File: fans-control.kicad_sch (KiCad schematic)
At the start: 47 parts, among them J2 PinHeader_1x4_P2.5mm_Drill1mm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, J3 PinHeader_1x4_P2.5mm_Drill1mm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, J4 PinHeader_1x4_P2.5mm_Drill1mm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, J5 PinHeader_1x4_P2.5mm_Drill1mm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, Q4 BSS138PW, U5 LM339_TSSOP_Split, U6 TS5A3359_VSSOP

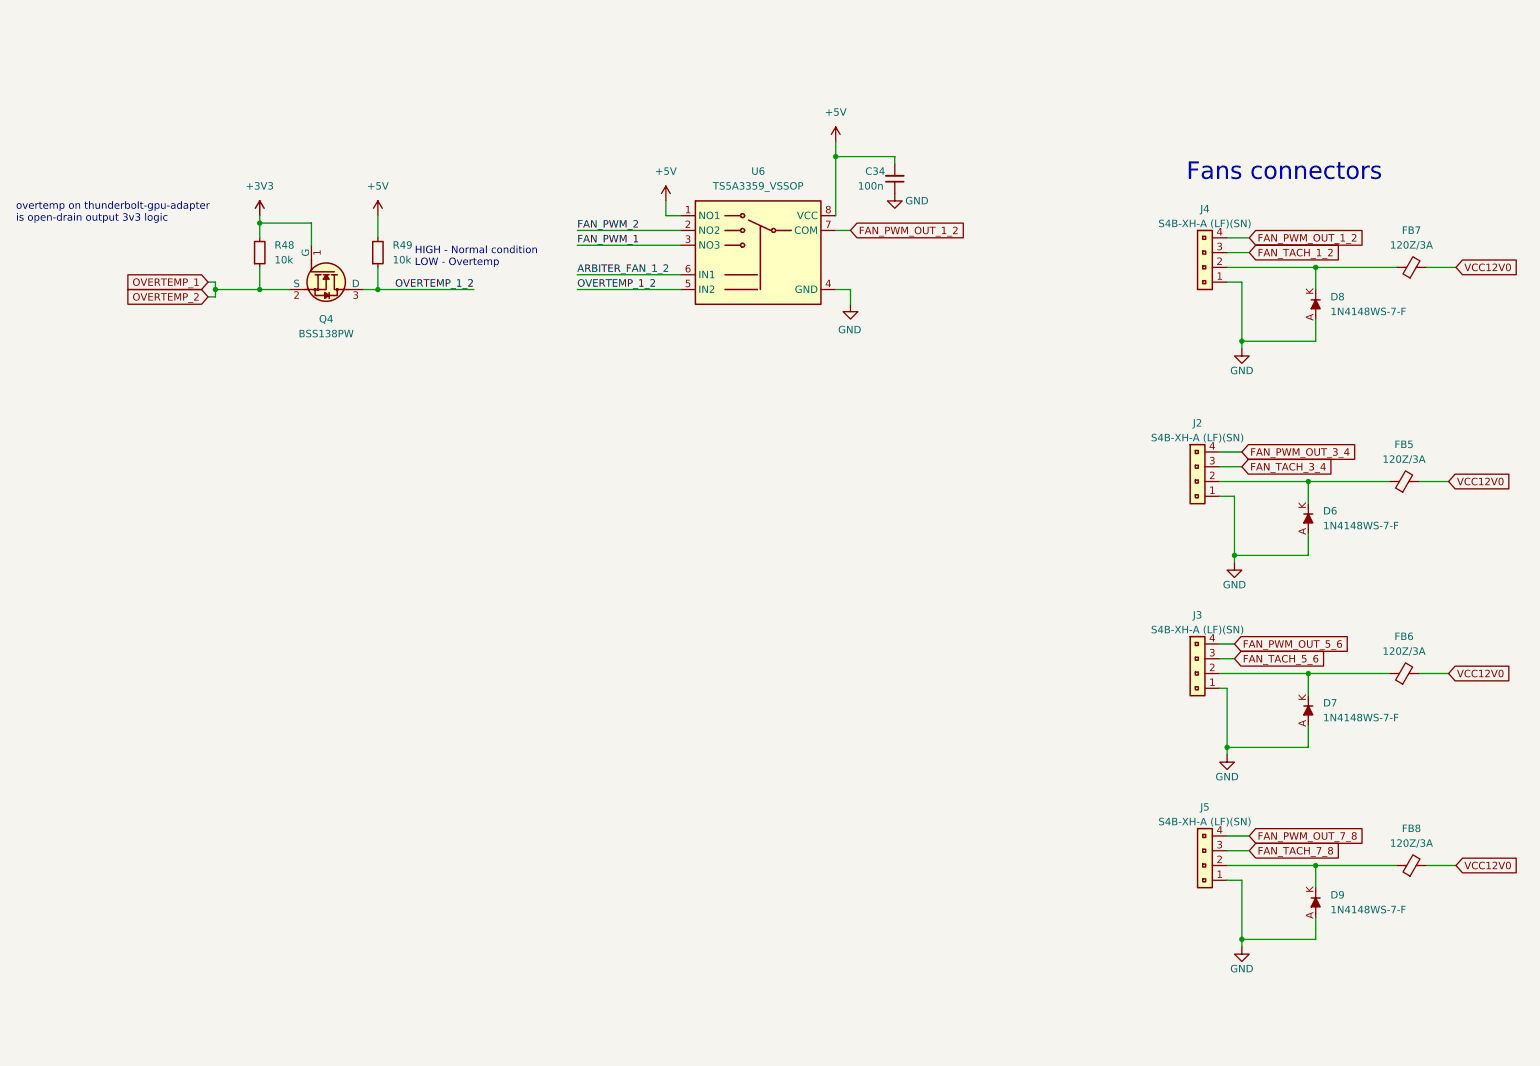
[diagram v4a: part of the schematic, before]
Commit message: Add fan arbiters for all outputs
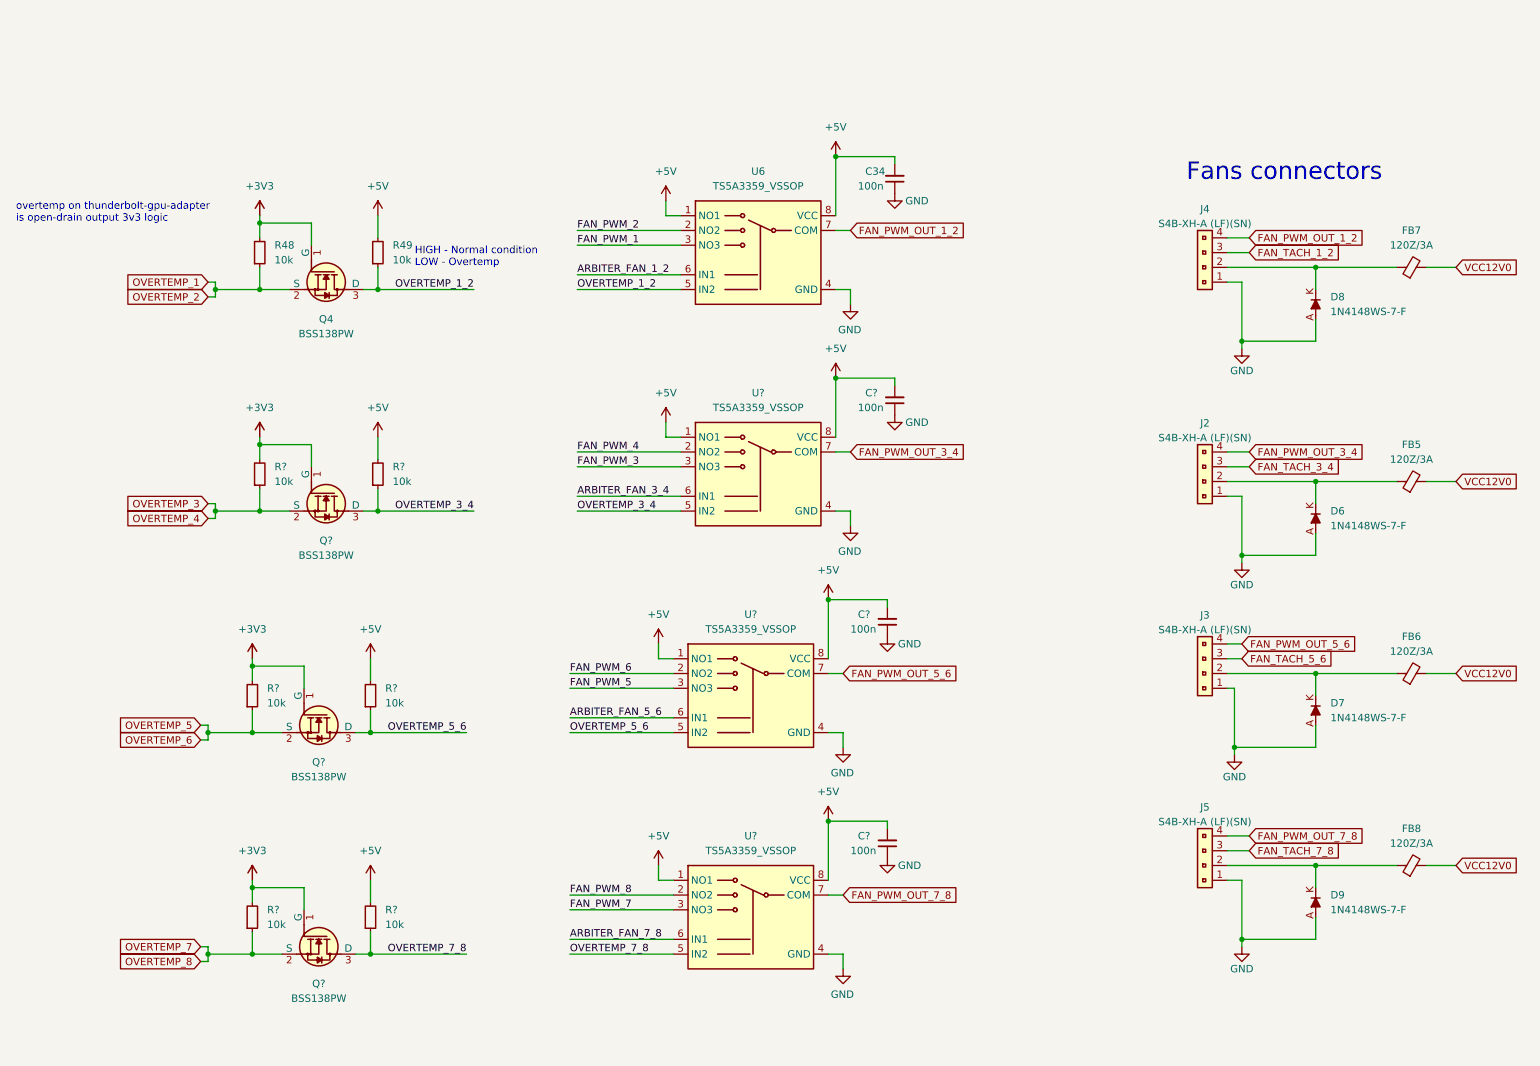
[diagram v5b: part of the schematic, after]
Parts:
- added C? (x3): C_100n_0402, antmicro-footprints:C_0402_1005Metric, symbol antmicroCapacitors0402:C_100n_0402
- added Q? (x3): BSS138PW, antmicro-footprints:SC70-3, symbol antmicroTransistorsFETsMOSFETsSingle:BSS138PW
- added R? (x6): R_10k_0402, antmicro-footprints:R_0402_1005Metric, symbol antmicroResistors0402:R_10k_0402
- added U? (x3): TS5A3359_VSSOP, antmicro-footprints:VSSOP-8_2.3x2mm_P0.5mm, symbol antmicroInterfaceAnalogSwitchesMultiplexersDemultiplexers:TS5A3359_VSSOP
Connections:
- net +3V3: now also Q?.1 (G), Q?.1 (G), Q?.1 (G), R?.2, R?.2, R?.2
- net +5V: now also C?.2, C?.2, C?.2, R?.2, R?.2, R?.2, U?.1 (NO1), U?.1 (NO1), U?.1 (NO1), U?.8 (VCC), U?.8 (VCC), U?.8 (VCC)
- net ARBITER_FAN_3_4: now also U?.6 (IN1)
- net ARBITER_FAN_5_6: now also U?.6 (IN1)
- net ARBITER_FAN_7_8: now also U?.6 (IN1)
- net FAN_PWM_3: now also U?.3 (NO3)
- net FAN_PWM_4: now also U?.2 (NO2)
- net FAN_PWM_5: now also U?.3 (NO3)
- net FAN_PWM_6: now also U?.2 (NO2)
- net FAN_PWM_7: now also U?.3 (NO3)
- net FAN_PWM_8: now also U?.2 (NO2)
- net FAN_PWM_OUT_3_4: now also U?.7 (COM)
- net FAN_PWM_OUT_5_6: now also U?.7 (COM)
- net FAN_PWM_OUT_7_8: now also U?.7 (COM)
- net GND: now also C?.1, C?.1, C?.1, U?.4 (GND), U?.4 (GND), U?.4 (GND)
- new net OVERTEMP_3: Q?.2 (S), R?.1
- new net OVERTEMP_3_4: Q?.3 (D), R?.1, U?.5 (IN2)
- new net OVERTEMP_5: Q?.2 (S), R?.1
- new net OVERTEMP_5_6: Q?.3 (D), R?.1, U?.5 (IN2)
- new net OVERTEMP_7: Q?.2 (S), R?.1
- new net OVERTEMP_7_8: Q?.3 (D), R?.1, U?.5 (IN2)
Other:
- moved on the sheet: D6, D7, FB5, FB6, J2, J3

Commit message: Reannotate
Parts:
- gave numbers to parts that had none: 15
- renumbered C34 to C36, D8 to D6, D6 to D7, D7 to D8, FB7 to FB5, FB5 to FB6, FB6 to FB7, J4 to J2, J2 to J3, J3 to J4, Q4 to Q6, R28 to R30, R29 to R31, R30 to R32, R31 to R33, R32 to R34, R33 to R35, R34 to R36, R35 to R37, R36 to R38, R37 to R39, R38 to R40, R39 to R41, R40 to R42, R41 to R43, R42 to R44, R43 to R45, R44 to R46, R45 to R47, R46 to R48, R47 to R49, R48 to R52, R49 to R56, U6 to U8

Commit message: Added control circuit for the casing fan
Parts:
- added C?: C_100n_0402, antmicro-footprints:C_0402_1005Metric, symbol antmicroCapacitors0402:C_100n_0402
- added R? (x16): R_0R_0603, antmicro-footprints:R_0603_1608Metric, symbol antmicroResistors0603:R_0R_0603
- added R?: R_10k_0402, antmicro-footprints:R_0402_1005Metric, symbol antmicroResistors0402:R_10k_0402
- added TP? (x3): TP_1mm_SMD, antmicro-footprints:TP_SMD_1mm, symbol antmicroTestPoints:TP_1mm_SMD
- added U?: MAX6643_QSOP, antmicro-footprints:QSOP-16_3x4.75x0.75mm_P0.5mm, symbol antmicroPMICMotorDriversControllers:MAX6643_QSOP
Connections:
- net +3V3: now also C?.2, R?.2, R?.2, R?.2, R?.2, R?.2, R?.2, R?.2, R?.2, U?.16 (VDD)
- net GND: now also C?.1, R?.1, R?.1, R?.1, R?.1, R?.1, R?.1, R?.1, R?.1, R?.1, U?.7 (GND)
- new net CASE_FAN_FAIL: TP?.1, U?.4 (~{FANFAIL})
- new net CASE_FAN_FULLSPD: TP?.1, U?.6 (FULLSPD)
- new net CASE_FAN_OT: TP?.1, U?.9 (~{OT})
- new net CASE_FAN_PWM: R?.2, U?.12 (PWM_OUT)
- new net CASE_FAN_TACH: U?.10 (FAN_IN2), U?.11 (FAN_IN1)
- new net CASE_TEMP_SENSE_1: U?.8 (DXP)
- new net CASE_TEMP_SENSE_2: R?.2
- new net FULLSPD: R?.1, R?.2
- new net OT1: R?.1, R?.2, U?.14 (OT1)
- new net OT2: R?.1, R?.2, U?.13 (OT2)
- new net TACHSET: R?.1, U?.5 (TACHSET)
- new net TH1: R?.1, R?.2, U?.1 (TH1)
- new net TH2: R?.1, R?.2, U?.15 (TH2)
- new net TL1: R?.1, R?.2, U?.3 (TL1)
- new net TL2: R?.1, R?.2, U?.2 (TL2)
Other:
- note added: "T_HIGH @ 60 DEG"
- note added: "T_LOW @ 30 DEG"
- note added: "T_OVER @ 80 DEG"
- moved on the sheet: C25, C26, C27, C28, C29, C30, C31, C32, C33, C34, C35, C36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

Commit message: Cosmetic changes and added adnotations
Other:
- note added: "Integrating circuit for finding higher PWM signal"
- note added: "Multiplexer for choosing higher PWM signal or 100% in case of overtemp"
- note added: "Voltage level translation for overtemp"
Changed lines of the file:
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@@
     (effects (font (size 1.27 1.27)) (justify left bottom))
+  )
+  (text "Multiplexer for choosing higher \nPWM signal or 100% in case of overtemp"
+    (at 244.475 41.275 0)
+    (effects (font (size 2 2)) (justify left bottom))
   )
   (text "HIGH - Normal condition\nLOW - Overtemp" (at 210.82 69.215 0)
@@
     (effects (font (size 1.54 1.54)) (justify left bottom))
   )
+  (text "Voltage level translation for overtemp" (at 166.37 45.085 0)
+    (effects (font (size 2 2)) (justify left bottom))
+  )
   (text "T_HIGH @ 60 DEG" (at 98.425 240.03 0)
     (effects (font (size 1.54 1.54)) (justify left bottom))
@@
     (effects (font (size 2.9972 2.9972)) (justify left bottom))
   )
+  (text "Integrating circuit for finding\nhigher PWM signal" (at 26.035 35.56 0)
+    (effects (font (size 2 2)) (justify left bottom))
+  )
   (text "overtemp on thunderbolt-gpu-adapter\nis open-drain output 3v3 logic"
